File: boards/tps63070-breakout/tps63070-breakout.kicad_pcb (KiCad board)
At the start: 2 copper layers, 24.7 x 22.9 mm, 15 parts, among them J1 MODULE PINS, U1 TPS63070

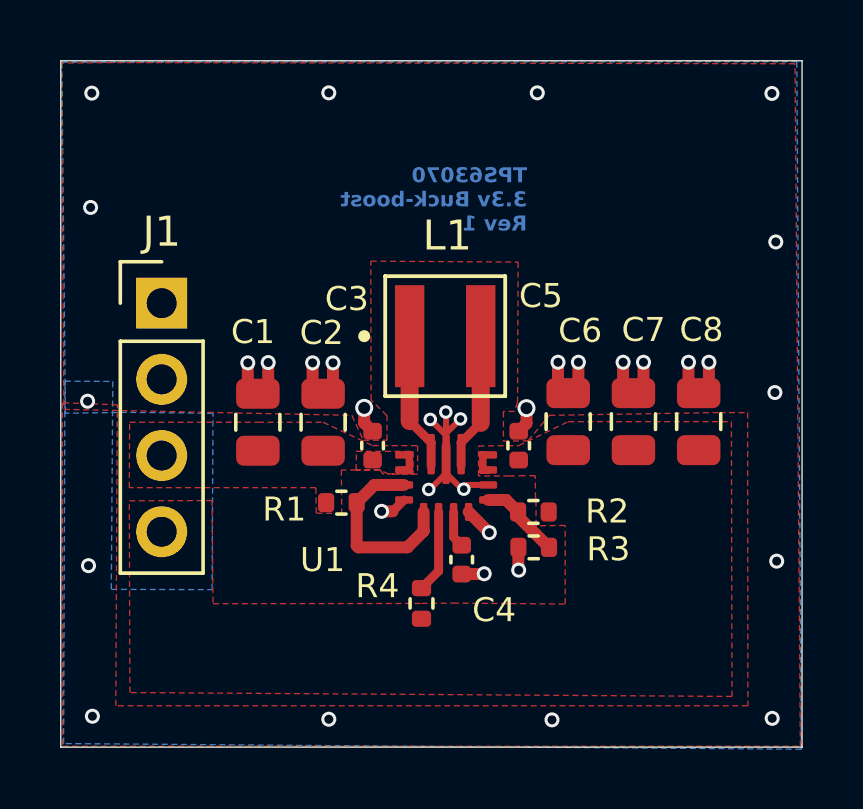
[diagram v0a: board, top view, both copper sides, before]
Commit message: fix(tps63070-breakout): repair symbol-lib rename fallout and clear fab DRC
- ERC: point sym-lib-table at the renamed TPS63070-Buck-Boost.kicad_sym
  and update the embedded symbol + lib_id to TPS63070RNMR, matching the
  devkit (the PR's library rename had left this board referencing the
  deleted TPS630701 file)
- Mark embedded TPS63070 footprint as SMD (matches library fix)
- fab DRC: bump silkscreen reference text to 1.0mm/0.15mm (JLCPCB/PCBWay
  advanced minimums) and relocate C3's reference out of L1's silkscreen
- fab DRC: PCBWay advanced requires 0.15mm pad-to-silk clearance, which
  stock KiCad 0402 footprints violate; add repo-local Passives.pretty
  variants of R/C_0402_1005Metric without the body silk lines and switch
  the seven 0402 parts to them (schematic + board)

ERC, DRC, and both fab DRC targets (jlcpcb/pcbway 2-layer advanced) pass.

Co-Authored-By: Claude Fable 5 <noreply@anthropic.com>
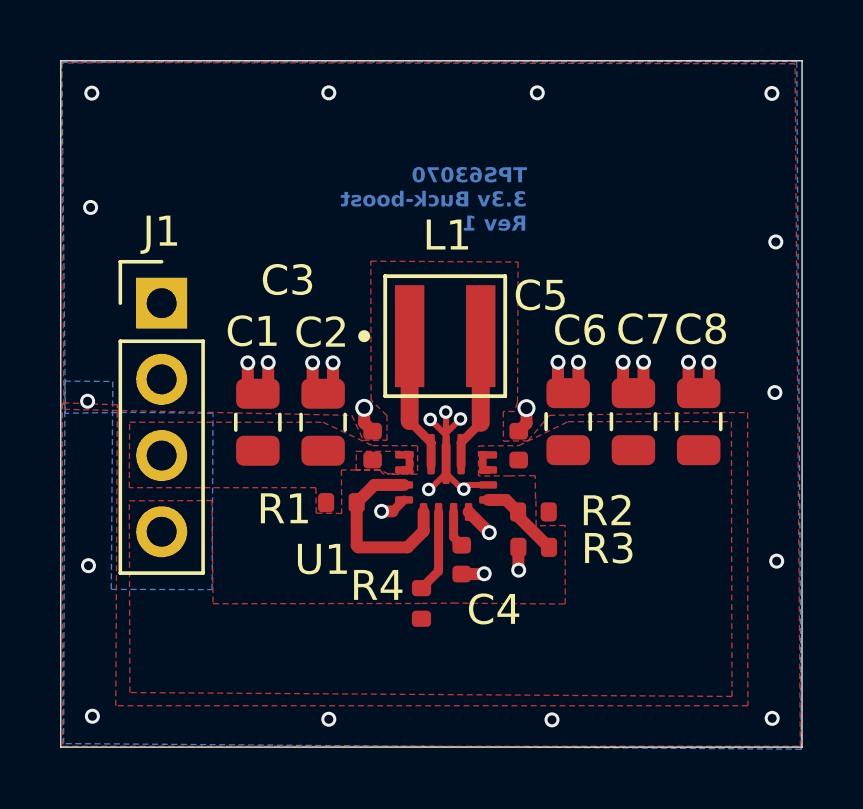
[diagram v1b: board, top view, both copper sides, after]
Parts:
- C3, C4, C5: footprint Capacitor_SMD:C_0402_1005Metric -> Passives:C_0402_1005Metric
- R1, R2, R3, R4: footprint Resistor_SMD:R_0402_1005Metric -> Passives:R_0402_1005Metric
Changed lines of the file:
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@@
 		)
 	)
-	(footprint "Capacitor_SMD:C_0402_1005Metric"
+	(footprint "Passives:C_0402_1005Metric"
 		(layer "F.Cu")
 		(at 64.82 55.3 90)
@@
 		(tags "capacitor")
 		(property "Reference" "C3"
-			(at 4.89 -0.86 0)
-			(layer "F.SilkS")
-			(effects
-				(font
-					(size 0.8 0.8)
-					(thickness 0.1)
+			(at 5.5 -2.82 0)
+			(layer "F.SilkS")
+			(effects
+				(font
+					(size 1 1)
+					(thickness 0.15)
 				)
 			)
@@
 		(attr smd)
 		(duplicate_pad_numbers_are_jumpers no)
-		(fp_line
-			(start -0.107836 -0.36)
-			(end 0.107836 -0.36)
-			(stroke
-				(width 0.12)
-				(type solid)
-			)
-			(layer "F.SilkS")
-		)
-		(fp_line
-			(start -0.107836 0.36)
-			(end 0.107836 0.36)
-			(stroke
-				(width 0.12)
-				(type solid)
-			)
-			(layer "F.SilkS")
-		)
 		(fp_rect
 			(start -0.91 -0.46)
@@
 			(effects
 				(font
-					(size 0.8 0.8)
-					(thickness 0.1)
+					(size 1 1)
+					(thickness 0.15)
 				)
 			)
@@
 		)
 	)
-	(footprint "Resistor_SMD:R_0402_1005Metric"
+	(footprint "Passives:R_0402_1005Metric"
 		(layer "F.Cu")
 		(at 63.78 57.2)
@@
 			(effects
 				(font
-					(size 0.8 0.8)
-					(thickness 0.1)
+					(size 1 1)
+					(thickness 0.15)
 				)
 			)
@@
 		(attr smd)
 		(duplicate_pad_numbers_are_jumpers no)
-		(fp_line
-			(start -0.153641 -0.38)
-			(end 0.153641 -0.38)
-			(stroke
-				(width 0.12)
-				(type solid)
-			)
-			(layer "F.SilkS")
-		)
-		(fp_line
-			(start -0.153641 0.38)
-			(end 0.153641 0.38)
-			(stroke
-				(width 0.12)
-				(type solid)
-			)
-			(layer "F.SilkS")
-		)
 		(fp_rect
 			(start -0.93 -0.47)
@@
 			(effects
 				(font
-					(size 0.8 0.8)
-					(thickness 0.1)
+					(size 1 1)
+					(thickness 0.15)
 				)
 			)
@@
 			(effects
 				(font
-					(size 0.8 0.8)
-					(thickness 0.1)
+					(size 1 1)
+					(thickness 0.15)
 				)
 			)
@@
 			(effects
 				(font
-					(size 0.8 0.8)
-					(thickness 0.1)
+					(size 1 1)
+					(thickness 0.15)
 				)
 			)
@@
 			)
 		)
-		(attr through_hole)
+		(attr smd)
 		(duplicate_pad_numbers_are_jumpers no)
 		(fp_poly
@@
 			(effects
 				(font
-					(size 0.8 0.8)
-					(thickness 0.1)
+					(size 1 1)
+					(thickness 0.15)
 				)
 			)
@@
 		)
 	)
-	(footprint "Capacitor_SMD:C_0402_1005Metric"
+	(footprint "Passives:C_0402_1005Metric"
 		(layer "F.Cu")
 		(at 69.69 55.3 90)
@@
 			(effects
 				(font
-					(size 0.8 0.8)
-					(thickness 0.1)
+					(size 1 1)
+					(thickness 0.15)
 				)
 			)
@@
 		(attr smd)
 		(duplicate_pad_numbers_are_jumpers no)
-		(fp_line
-			(start -0.107836 -0.36)
-			(end 0.107836 -0.36)
-			(stroke
-				(width 0.12)
-				(type solid)
-			)
-			(layer "F.SilkS")
-		)
-		(fp_line
-			(start -0.107836 0.36)
-			(end 0.107836 0.36)
-			(stroke
-				(width 0.12)
-				(type solid)
-			)
-			(layer "F.SilkS")
-		)
 		(fp_rect
 			(start -0.91 -0.46)
@@
 			(effects
 				(font
-					(size 0.8 0.8)
-					(thickness 0.1)
+					(size 1 1)
+					(thickness 0.15)
 				)
 			)
@@
 		)
 	)
-	(footprint "Resistor_SMD:R_0402_1005Metric"
+	(footprint "Passives:R_0402_1005Metric"
 		(layer "F.Cu")
 		(at 66.45 60.56 90)
@@
 			(effects
 				(font
-					(size 0.8 0.8)
-					(thickness 0.1)
+					(size 1 1)
+					(thickness 0.15)
 				)
 			)
@@
 		(attr smd)
 		(duplicate_pad_numbers_are_jumpers no)
-		(fp_line
-			(start -0.153641 -0.38)
-			(end 0.153641 -0.38)
-			(stroke
-				(width 0.12)
-				(type solid)
-			)
-			(layer "F.SilkS")
-		)
-		(fp_line
-			(start -0.153641 0.38)
-			(end 0.153641 0.38)
-			(stroke
-				(width 0.12)
-				(type solid)
-			)
-			(layer "F.SilkS")
-		)
 		(fp_rect
 			(start -0.93 -0.47)
@@
 		)
 	)
-	(footprint "Capacitor_SMD:C_0402_1005Metric"
+	(footprint "Passives:C_0402_1005Metric"
 		(layer "F.Cu")
 		(at 67.79 59.1 -90)
@@
 			(effects
 				(font
-					(size 0.8 0.8)
-					(thickness 0.1)
+					(size 1 1)
+					(thickness 0.15)
 				)
 			)
@@
 		(attr smd)
 		(duplicate_pad_numbers_are_jumpers no)
-		(fp_line
-			(start -0.107836 0.36)
-			(end 0.107836 0.36)
-			(stroke
-				(width 0.12)
-				(type solid)
-			)
-			(layer "F.SilkS")
-		)
-		(fp_line
-			(start -0.107836 -0.36)
-			(end 0.107836 -0.36)
-			(stroke
-				(width 0.12)
-				(type solid)
-			)
-			(layer "F.SilkS")
-		)
 		(fp_rect
 			(start -0.91 -0.46)
@@
 		)
 	)
-	(footprint "Resistor_SMD:R_0402_1005Metric"
+	(footprint "Passives:R_0402_1005Metric"
 		(layer "F.Cu")
 		(at 70.18 57.51 180)
@@
 			(effects
 				(font
-					(size 0.8 0.8)
-					(thickness 0.1)
+					(size 1 1)
+					(thickness 0.15)
 				)
 			)
@@
 		(attr smd)
 		(duplicate_pad_numbers_are_jumpers no)
-		(fp_line
-			(start -0.153641 0.38)
-			(end 0.153641 0.38)
-			(stroke
-				(width 0.12)
-				(type solid)
-			)
-			(layer "F.SilkS")
-		)
-		(fp_line
-			(start -0.153641 -0.38)
-			(end 0.153641 -0.38)
-			(stroke
-				(width 0.12)
-				(type solid)
-			)
-			(layer "F.SilkS")
-		)
 		(fp_rect
 			(start -0.93 -0.47)
@@
 		)
 	)
-	(footprint "Resistor_SMD:R_0402_1005Metric"
+	(footprint "Passives:R_0402_1005Metric"
 		(layer "F.Cu")
 		(at 70.19 58.69 180)
@@
 			(effects
 				(font
-					(size 0.8 0.8)
-					(thickness 0.1)
+					(size 1 1)
+					(thickness 0.15)
 				)
 			)
@@
 		(attr smd)
 		(duplicate_pad_numbers_are_jumpers no)
-		(fp_line
-			(start -0.153641 0.38)
-			(end 0.153641 0.38)
-			(stroke
-				(width 0.12)
-				(type solid)
-			)
-			(layer "F.SilkS")
-		)
-		(fp_line
-			(start -0.153641 -0.38)
-			(end 0.153641 -0.38)
-			(stroke
-				(width 0.12)
-				(type solid)
-			)
-			(layer "F.SilkS")
-		)
 		(fp_rect
 			(start -0.93 -0.47)
